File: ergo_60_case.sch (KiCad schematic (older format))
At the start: 21 parts, among them SW1 SW_Push, U1 PRTR5V0U2X, U2 OLED_SSD1306, U3 AT90USB1286-AU, U4 AVR-ISP, Y1 16MHz

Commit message: corrected mising +5v trace and funky looking schematic on led 56
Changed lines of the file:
@@
 	1    0    0    -1
 $EndComp
-Text GLabel 7050 1875 0    50   Input ~ 0
-LEDDATA
 $Sheet
 S 9375 5975 625  450

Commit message: updates for prod
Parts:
- U2: footprint KiCadLibs:SSD1306_128x64OLED_wHoles -> KiCadLibs:SSD1306_128x64OLED
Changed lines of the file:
@@
 F 0 "U2" H 9125 4890 50  0000 C CNN
 F 1 "OLED_SSD1306" H 9125 4799 50  0000 C CNN
-F 2 "KiCadLibs:SSD1306_128x64OLED_wHoles" H 9200 4825 50  0001 C CNN
+F 2 "KiCadLibs:SSD1306_128x64OLED" H 9200 4825 50  0001 C CNN
 F 3 "" H 9200 4825 50  0001 C CNN
 	1    9100 4575

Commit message: correct mcu processor footprint
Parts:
- added LED1, LED3: LED_Strip, KiCadLibs:StripLED, symbol Keeb:LED_Strip
- added LED2: LED_Strip, KiCadLibs:StripLED_BackOnly, symbol Keeb:LED_Strip
- U2: footprint KiCadLibs:SSD1306_128x64OLED -> KiCadLibs:SSD1306_128x64OLED_wHoles
- U3: footprint KiCadLibs:AT90USB1286-AUQFP50P1200X1200X120-64N -> KiCadLibs:AT90USB1286-AU_QFP80P1600X1600X120-64N
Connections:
- net GND: now also LED1.1 (Pin_1), LED2.1 (Pin_1), LED3.1 (Pin_1)
- net LEDDATA: now also LED1.2 (Pin_2), LED2.2 (Pin_2), LED3.2 (Pin_2)
- net VCC: now also LED1.3 (Pin_3), LED2.3 (Pin_3), LED3.3 (Pin_3)
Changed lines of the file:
@@
 F 0 "U2" H 9125 4890 50  0000 C CNN
 F 1 "OLED_SSD1306" H 9125 4799 50  0000 C CNN
-F 2 "KiCadLibs:SSD1306_128x64OLED" H 9200 4825 50  0001 C CNN
+F 2 "KiCadLibs:SSD1306_128x64OLED_wHoles" H 9200 4825 50  0001 C CNN
 F 3 "" H 9200 4825 50  0001 C CNN
 	1    9100 4575
@@
 Wire Wire Line
 	2875 1500 3675 1500
-$Comp
-L power:+5V #PWR0114
-U 1 1 6007E379
-P 4750 2875
-F 0 "#PWR0114" H 4750 2725 50  0001 C CNN
-F 1 "+5V" H 4765 3048 50  0000 C CNN
-F 2 "" H 4750 2875 50  0001 C CNN
-F 3 "" H 4750 2875 50  0001 C CNN
-	1    4750 2875
-	1    0    0    -1
-$EndComp
-Wire Wire Line
-	4750 2875 4750 3075
-Wire Wire Line
-	4750 3075 4050 3075
 Wire Wire Line
 	4050 3075 4050 3175
-Connection ~ 4750 3075
 $Comp
 L power:+5V #PWR0115
@@
 F 0 "U3" H 5275 2986 50  0000 C CNN
 F 1 "AT90USB1286-AU" H 5275 2895 50  0000 C CNN
-F 2 "KiCadLibs:AT90USB1286-AUQFP50P1200X1200X120-64N" H 5275 5075 50  0001 C CIN
+F 2 "KiCadLibs:AT90USB1286-AU_QFP80P1600X1600X120-64N" H 5275 5075 50  0001 C CIN
 F 3 "http://ww1.microchip.com/downloads/en/DeviceDoc/doc7593.pdf" H 5275 5075 50  0001 C CNN
 	1    5275 5075
 	1    0    0    -1
 $EndComp
-Wire Wire Line
-	4750 3075 5175 3075
 Wire Wire Line
 	5275 3075 5375 3075
@@
 Text GLabel 4675 5875 0    50   Input ~ 0
 LEDDATA
+Text GLabel 7175 2150 0    50   Input ~ 0
+LEDDATA
+Text GLabel 7175 2775 0    50   Input ~ 0
+LEDDATA
+$Comp
+L power:GND #PWR0123
+U 1 1 6037EABB
+P 7175 2250
+F 0 "#PWR0123" H 7175 2000 50  0001 C CNN
+F 1 "GND" H 7180 2077 50  0000 C CNN
+F 2 "" H 7175 2250 50  0001 C CNN
+F 3 "" H 7175 2250 50  0001 C CNN
+	1    7175 2250
+	1    0    0    -1
+$EndComp
+$Comp
+L power:GND #PWR0124
+U 1 1 60381849
+P 7175 2875
+F 0 "#PWR0124" H 7175 2625 50  0001 C CNN
+F 1 "GND" H 7180 2702 50  0000 C CNN
+F 2 "" H 7175 2875 50  0001 C CNN
+F 3 "" H 7175 2875 50  0001 C CNN
+	1    7175 2875
+	1    0    0    -1
+$EndComp
+Connection ~ 4750 3075
+Wire Wire Line
+	4750 3075 5175 3075
+Wire Wire Line
+	4750 3075 4050 3075
+Wire Wire Line
+	4750 2875 4750 3075
+$Comp
+L power:+5V #PWR0114
+U 1 1 6007E379
+P 4750 2875
+F 0 "#PWR0114" H 4750 2725 50  0001 C CNN
+F 1 "+5V" H 4765 3048 50  0000 C CNN
+F 2 "" H 4750 2875 50  0001 C CNN
+F 3 "" H 4750 2875 50  0001 C CNN
+	1    4750 2875
+	1    0    0    -1
+$EndComp
+$Comp
+L power:VCC #PWR0125
+U 1 1 603957EA
+P 7175 2050
+F 0 "#PWR0125" H 7175 1900 50  0001 C CNN
+F 1 "VCC" H 7192 2223 50  0000 C CNN
+F 2 "" H 7175 2050 50  0001 C CNN
+F 3 "" H 7175 2050 50  0001 C CNN
+	1    7175 2050
+	1    0    0    -1
+$EndComp
+$Comp
+L power:VCC #PWR0126
+U 1 1 6039EC7C
+P 7175 2675
+F 0 "#PWR0126" H 7175 2525 50  0001 C CNN
+F 1 "VCC" H 7192 2848 50  0000 C CNN
+F 2 "" H 7175 2675 50  0001 C CNN
+F 3 "" H 7175 2675 50  0001 C CNN
+	1    7175 2675
+	1    0    0    -1
+$EndComp
+$Comp
+L Keeb:LED_Strip LED1
+U 1 1 603A35ED
+P 7375 2150
+F 0 "LED1" H 7295 2100 50  0000 R CNN
+F 1 "LED_Strip" H 7295 2191 50  0000 R CNN
+F 2 "KiCadLibs:StripLED" H 7375 2150 50  0001 C CNN
+F 3 "" H 7375 2150 50  0001 C CNN
+	1    7375 2150
+	-1   0    0    1
+$EndComp
+$Comp
+L Keeb:LED_Strip LED2
+U 1 1 603A4B22
+P 7375 2775
+F 0 "LED2" H 7295 2725 50  0000 R CNN
+F 1 "LED_Strip" H 7295 2816 50  0000 R CNN
+F 2 "KiCadLibs:StripLED_BackOnly" H 7375 2775 50  0001 C CNN
+F 3 "" H 7375 2775 50  0001 C CNN
+	1    7375 2775
+	-1   0    0    1
+$EndComp
+Text GLabel 7175 3425 0    50   Input ~ 0
+LEDDATA
+$Comp
+L power:GND #PWR0127
+U 1 1 6040DB23
+P 7175 3525
+F 0 "#PWR0127" H 7175 3275 50  0001 C CNN
+F 1 "GND" H 7180 3352 50  0000 C CNN
+F 2 "" H 7175 3525 50  0001 C CNN
+F 3 "" H 7175 3525 50  0001 C CNN
+	1    7175 3525
+	1    0    0    -1
+$EndComp
+$Comp
+L power:VCC #PWR0128
+U 1 1 6040DB2D
+P 7175 3325
+F 0 "#PWR0128" H 7175 3175 50  0001 C CNN
+F 1 "VCC" H 7192 3498 50  0000 C CNN
+F 2 "" H 7175 3325 50  0001 C CNN
+F 3 "" H 7175 3325 50  0001 C CNN
+	1    7175 3325
+	1    0    0    -1
+$EndComp
+$Comp
+L Keeb:LED_Strip LED3
+U 1 1 6040DB37
+P 7375 3425
+F 0 "LED3" H 7295 3375 50  0000 R CNN
+F 1 "LED_Strip" H 7295 3466 50  0000 R CNN
+F 2 "KiCadLibs:StripLED" H 7375 3425 50  0001 C CNN
+F 3 "" H 7375 3425 50  0001 C CNN
+	1    7375 3425
+	-1   0    0    1
+$EndComp
 $EndSCHEMATC

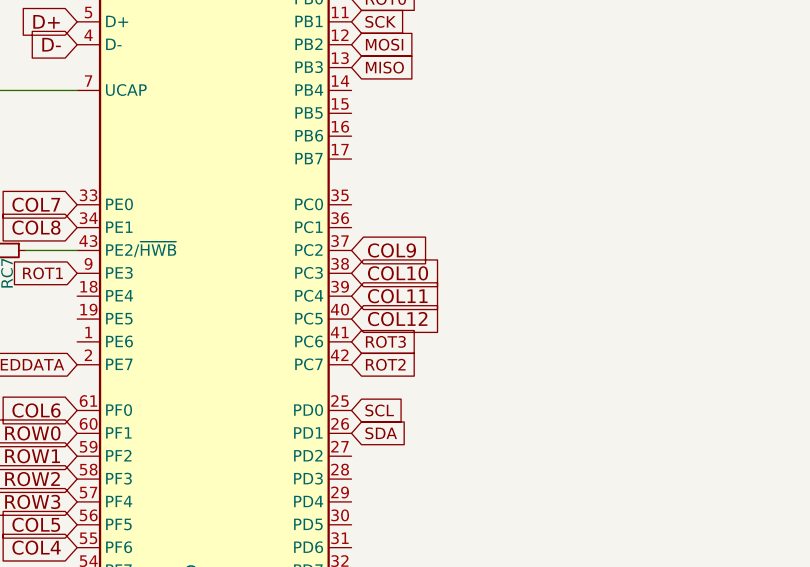
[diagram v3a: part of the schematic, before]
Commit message: making more clearance
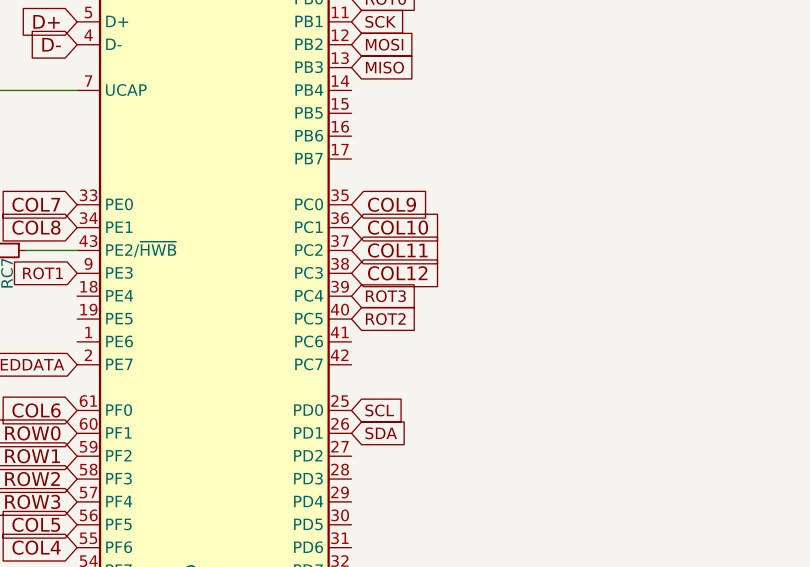
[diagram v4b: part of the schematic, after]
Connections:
- net COL10: now also U3.36 (PC1); no longer U3.38 (PC3)
- net COL11: now also U3.37 (PC2); no longer U3.39 (PC4)
- net COL12: now also U3.38 (PC3); no longer U3.40 (PC5)
- net COL9: now also U3.35 (PC0); no longer U3.37 (PC2)
- net ROT2: now also U3.40 (PC5); no longer U3.42 (PC7)
- net ROT3: now also U3.39 (PC4); no longer U3.41 (PC6)
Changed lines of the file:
@@
 Text GLabel 4675 5275 0    60   Input ~ 0
 COL8
+Text GLabel 5875 5175 2    60   Input ~ 0
+COL9
+Text GLabel 5875 5275 2    60   Input ~ 0
+COL10
 Text GLabel 5875 5375 2    60   Input ~ 0
-COL9
+COL11
 Text GLabel 5875 5475 2    60   Input ~ 0
-COL10
-Text GLabel 5875 5575 2    60   Input ~ 0
-COL11
-Text GLabel 5875 5675 2    60   Input ~ 0
 COL12
 Text GLabel 5875 3675 2    60   Input ~ 0
@@
 Text GLabel 4675 5475 0    50   Input ~ 0
 ROT1
-Text GLabel 5875 5875 2    50   Input ~ 0
-ROT2
-Text GLabel 5875 5775 2    50   Input ~ 0
-ROT3
 Text GLabel 4675 5875 0    50   Input ~ 0
 LEDDATA
@@
 	-1   0    0    1
 $EndComp
+Text GLabel 5875 5575 2    50   Input ~ 0
+ROT3
+Text GLabel 5875 5675 2    50   Input ~ 0
+ROT2
 $EndSCHEMATC

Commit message: updating footprints for proper clearance
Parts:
- U3: footprint KiCadLibs:AT90USB1286-AU_QFP80P1600X1600X120-64N -> KiCadLibs:AT90USB1286-AU_TQFP_16X16-64N
- USB1: footprint Type-C:HRO-TYPE-C-31-M-12-Assembly -> KiCadLibs:HRO-TYPE-C-31-M-12_.25clearance
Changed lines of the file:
@@
 F 0 "USB1" H 1931 2347 60  0000 C CNN
 F 1 "HRO-TYPE-C-31-M-12" H 1931 2241 60  0000 C CNN
-F 2 "Type-C:HRO-TYPE-C-31-M-12-Assembly" H 2100 1550 60  0001 C CNN
+F 2 "KiCadLibs:HRO-TYPE-C-31-M-12_.25clearance" H 2100 1550 60  0001 C CNN
 F 3 "" H 2100 1550 60  0001 C CNN
 	1    2100 1550
@@
 F 0 "U3" H 5275 2986 50  0000 C CNN
 F 1 "AT90USB1286-AU" H 5275 2895 50  0000 C CNN
-F 2 "KiCadLibs:AT90USB1286-AU_QFP80P1600X1600X120-64N" H 5275 5075 50  0001 C CIN
+F 2 "KiCadLibs:AT90USB1286-AU_TQFP_16X16-64N" H 5275 5075 50  0001 C CIN
 F 3 "http://ww1.microchip.com/downloads/en/DeviceDoc/doc7593.pdf" H 5275 5075 50  0001 C CNN
 	1    5275 5075
